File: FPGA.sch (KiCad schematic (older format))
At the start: 5 parts, among them U34 PCA9555AHF, U39 PCA9555AHF

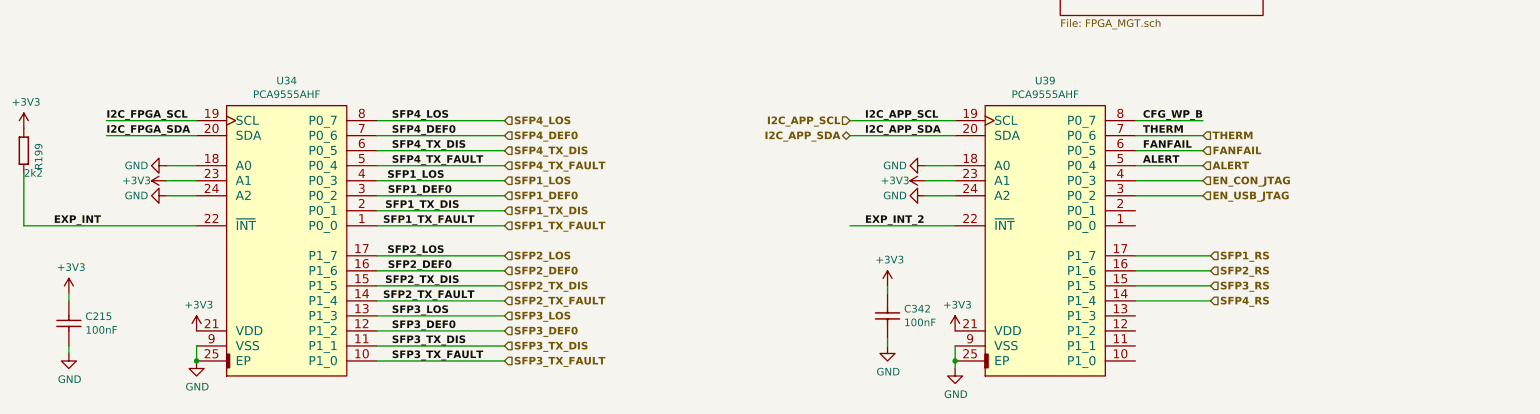
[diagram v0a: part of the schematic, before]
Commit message: LEDs and button added, routed other signals
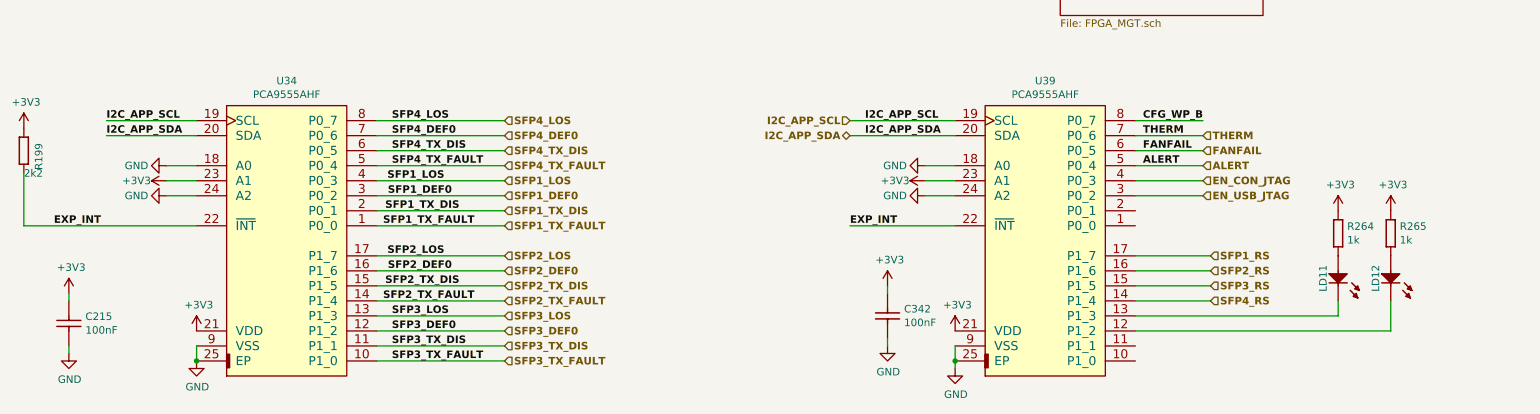
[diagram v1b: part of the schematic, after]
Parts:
- added LD11, LD12: LED_AVAGO_HSMC-C120, ICs And Semiconductors SMD:LED_AVAGO_HSMC-C120, symbol LEDs_&_Displays:LED_AVAGO_HSMC-C120
- added R264, R265: R0402_1K_1%_0.0625W_100PPM, RESC1005X40N, symbol Resistors_SMD:R0402_1K_1%_0.0625W_100PPM
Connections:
- net EXP_INT_2 is gone; now on net EXP_INT: U39.22 (~INT)
- net +3V3: now also R264.1, R265.1
- net I2C_APP_SCL: now also U34.19 (SCL)
- net I2C_APP_SDA: now also U34.20 (SDA)
- net I2C_FPGA_SCL: no longer U34.19 (SCL)
- net I2C_FPGA_SDA: no longer U34.20 (SDA)
- net at U39.12 (P1_2): now also LD12.1 (C)
- net at U39.13 (P1_3): now also LD11.1 (C)
- new net: LD11.2 (A), R264.2
- new net: LD12.2 (A), R265.2

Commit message: bugs fixed
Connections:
- net +3V3: now also U39.18 (A0); no longer U39.23 (A1)
- net GND: now also U39.23 (A1); no longer U39.18 (A0)
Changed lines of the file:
@@
 F0 "FPGA_13_14" 50
 F1 "FPGA_13_14.sch" 50
-F2 "FMC1_N_LA_[0..33]" I R 11450 1850 50
-F3 "FMC1_P_LA_[0..33]" I R 11450 1950 50
-F4 "FMC2_N_LA_[0..33]" I R 11450 2150 50
-F5 "FMC2_P_LA_[0..33]" I R 11450 2250 50
-F6 "CCLK" I L 9950 2100 50
-F7 "CFG_WP_B" O L 9950 2200 50
-F8 "FMC1_CLK1_M2C_P" I R 11450 2700 50
-F9 "FMC1_CLK1_M2C_N" I R 11450 2800 50
-F10 "FMC1_CLK0_M2C_P" I R 11450 2900 50
-F11 "FMC1_CLK0_M2C_N" I R 11450 3000 50
+F2 "CCLK" I L 9950 2100 50
+F3 "CFG_WP_B" O L 9950 2200 50
+F4 "FMC1_CLK1_M2C_P" I R 11450 2700 50
+F5 "FMC1_CLK1_M2C_N" I R 11450 2800 50
+F6 "FMC1_CLK0_M2C_P" I R 11450 2900 50
+F7 "FMC1_CLK0_M2C_N" I R 11450 3000 50
 $EndSheet
 Text HLabel 1750 2050 0    50   BiDi ~ 10
@@
 L power:+3V3 #PWR?
 U 1 1 5C5ED5B2
-P 7100 8750
+P 7100 8650
 AR Path="/5BD32060/5C5ED5B2" Ref="#PWR?"  Part="1"
 AR Path="/5C907554/5C417BCB/5C5ED5B2" Ref="#PWR?"  Part="1"
 AR Path="/5C907554/5C5ED5B2" Ref="#PWR0117"  Part="1"
 AR Path="/5C907554/5CAAC367/5C5ED5B2" Ref="#PWR?"  Part="1"
-F 0 "#PWR0117" H 7100 8600 50  0001 C CNN
-F 1 "+3V3" V 7100 8950 50  0000 C CNN
-F 2 "" H 7100 8750 50  0001 C CNN
-F 3 "" H 7100 8750 50  0001 C CNN
-	1    7100 8750
+F 0 "#PWR0117" H 7100 8500 50  0001 C CNN
+F 1 "+3V3" V 7100 8850 50  0000 C CNN
+F 2 "" H 7100 8650 50  0001 C CNN
+F 3 "" H 7100 8650 50  0001 C CNN
+	1    7100 8650
 	0    -1   -1   0
 $EndComp
@@
 L power:GND #PWR?
 U 1 1 5C5ED5BE
-P 7100 8650
+P 7100 8750
 AR Path="/5BD32060/5C5ED5BE" Ref="#PWR?"  Part="1"
 AR Path="/5BABAC65/5C5ED5BE" Ref="#PWR?"  Part="1"
@@
 AR Path="/5C907554/5C417BCB/5C5ED5BE" Ref="#PWR?"  Part="1"
 AR Path="/5C907554/5C5ED5BE" Ref="#PWR0115"  Part="1"
-F 0 "#PWR0115" H 7100 8400 50  0001 C CNN
-F 1 "GND" V 7100 8450 50  0000 C CNN
-F 2 "" H 7100 8650 50  0001 C CNN
-F 3 "" H 7100 8650 50  0001 C CNN
-	1    7100 8650
+F 0 "#PWR0115" H 7100 8500 50  0001 C CNN
+F 1 "GND" V 7100 8550 50  0000 C CNN
+F 2 "" H 7100 8750 50  0001 C CNN
+F 3 "" H 7100 8750 50  0001 C CNN
+	1    7100 8750
 	0    1    1    0
 $EndComp

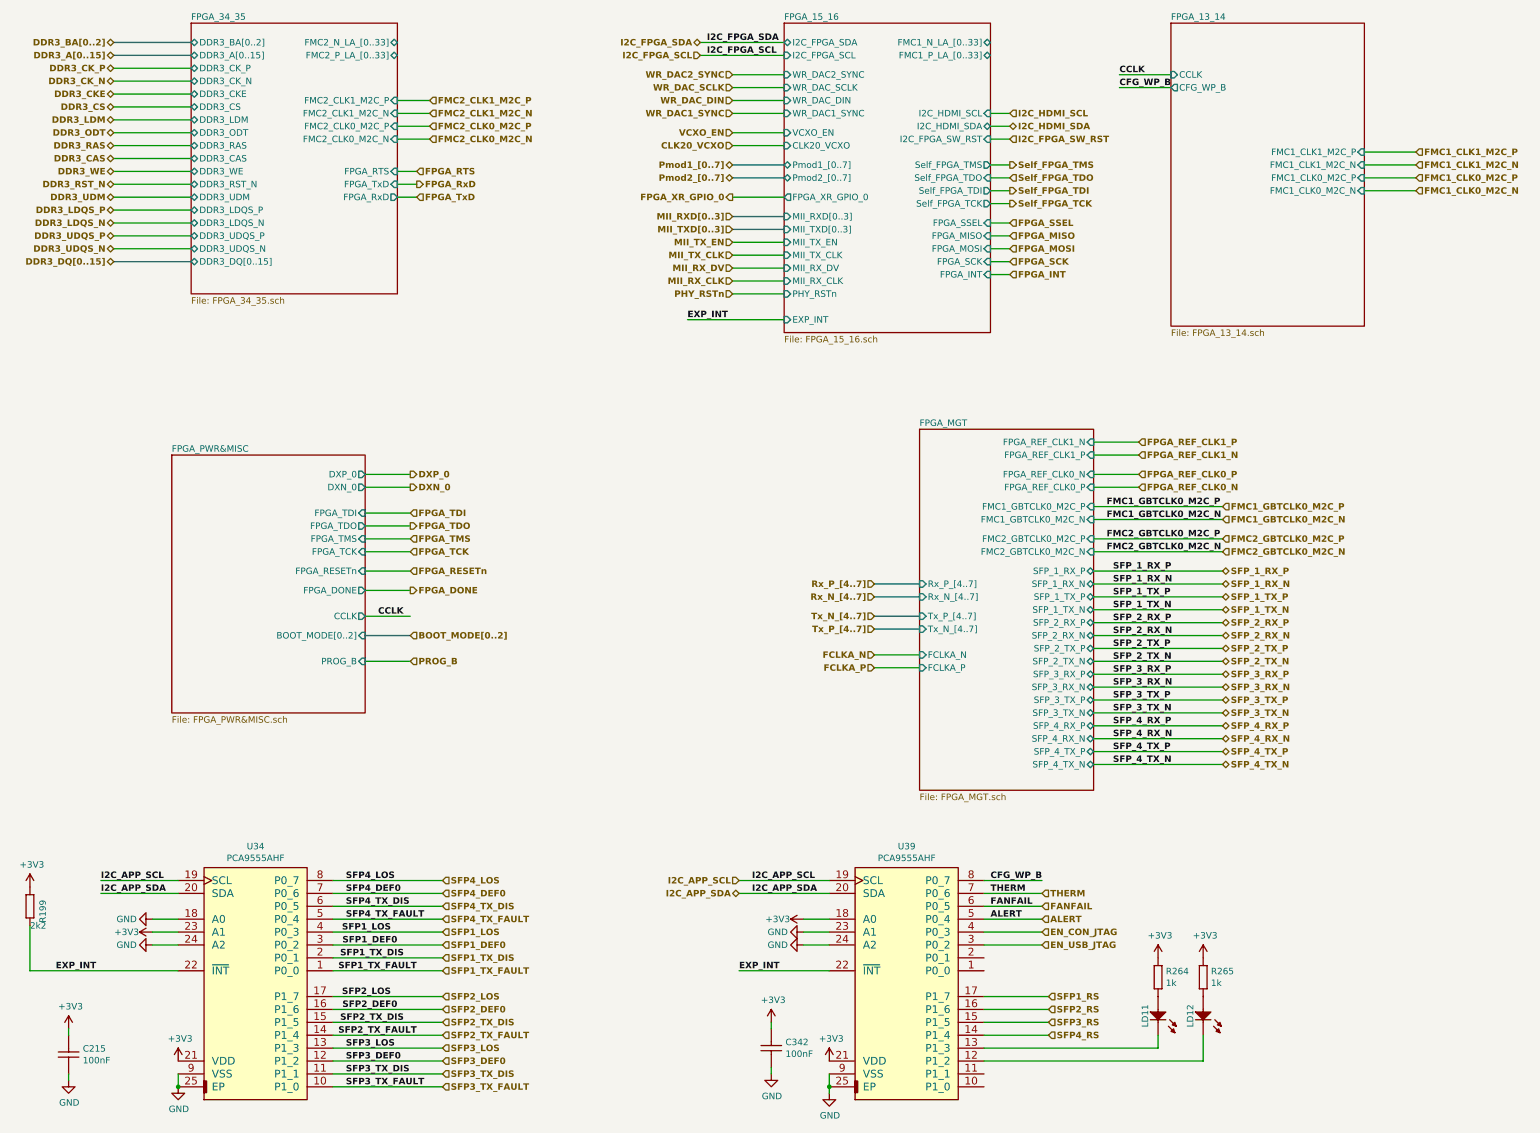
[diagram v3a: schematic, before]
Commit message: new FMC JTAG chain
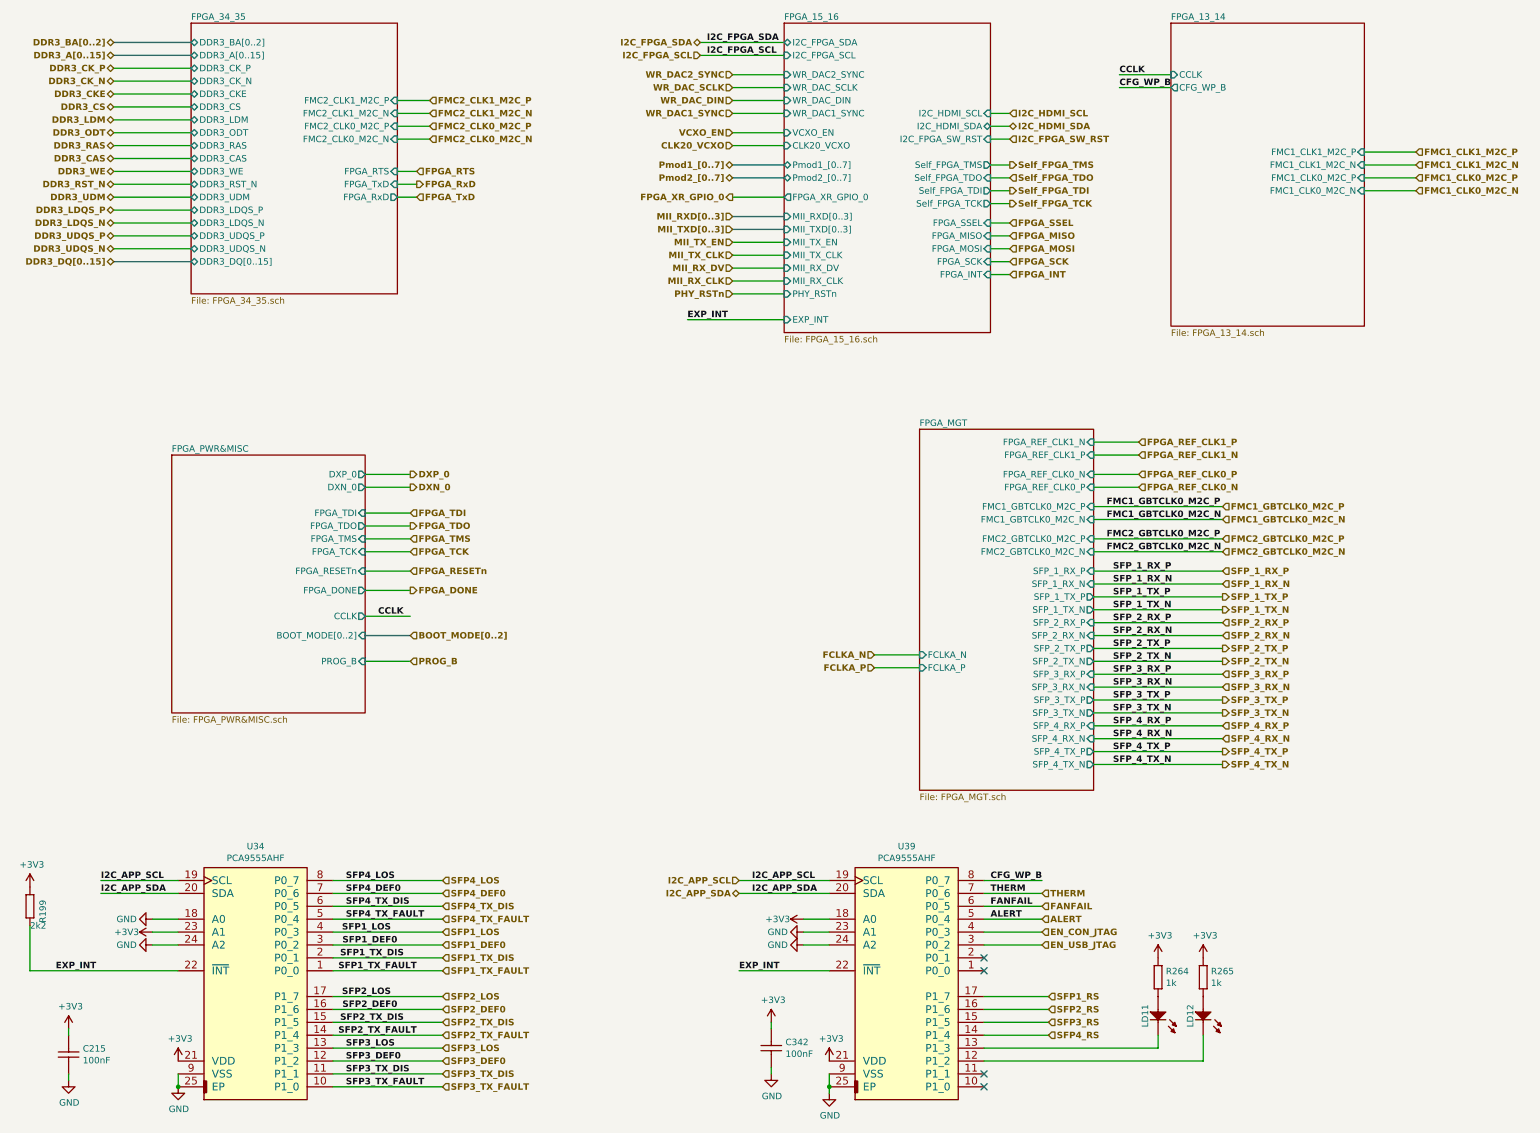
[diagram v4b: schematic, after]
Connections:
- no-connect marks 0 -> 4
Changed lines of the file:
@@
 F8 "FMC2_GBTCLK0_M2C_P" I R 9350 5700 50
 F9 "FMC2_GBTCLK0_M2C_N" I R 9350 5800 50
-F10 "SFP_1_RX_P" B R 9350 5950 50
-F11 "SFP_1_RX_N" B R 9350 6050 50
-F12 "SFP_1_TX_P" B R 9350 6150 50
-F13 "SFP_1_TX_N" B R 9350 6250 50
-F14 "SFP_2_RX_P" B R 9350 6350 50
-F15 "SFP_2_RX_N" B R 9350 6450 50
-F16 "SFP_2_TX_P" B R 9350 6550 50
-F17 "SFP_2_TX_N" B R 9350 6650 50
-F18 "SFP_3_RX_P" B R 9350 6750 50
-F19 "SFP_3_RX_N" B R 9350 6850 50
-F20 "SFP_3_TX_P" B R 9350 6950 50
-F21 "SFP_3_TX_N" B R 9350 7050 50
-F22 "SFP_4_RX_P" B R 9350 7150 50
-F23 "SFP_4_RX_N" B R 9350 7250 50
-F24 "SFP_4_TX_P" B R 9350 7350 50
-F25 "SFP_4_TX_N" B R 9350 7450 50
-F26 "Rx_P_[4..7]" I L 8000 6050 50
-F27 "Rx_N_[4..7]" I L 8000 6150 50
-F28 "Tx_P_[4..7]" I L 8000 6300 50
-F29 "Tx_N_[4..7]" I L 8000 6400 50
+F10 "SFP_1_RX_P" I R 9350 5950 50
+F11 "SFP_1_RX_N" I R 9350 6050 50
+F12 "SFP_1_TX_P" O R 9350 6150 50
+F13 "SFP_1_TX_N" O R 9350 6250 50
+F14 "SFP_2_RX_P" I R 9350 6350 50
+F15 "SFP_2_RX_N" I R 9350 6450 50
+F16 "SFP_2_TX_P" O R 9350 6550 50
+F17 "SFP_2_TX_N" O R 9350 6650 50
+F18 "SFP_3_RX_P" I R 9350 6750 50
+F19 "SFP_3_RX_N" I R 9350 6850 50
+F20 "SFP_3_TX_P" O R 9350 6950 50
+F21 "SFP_3_TX_N" O R 9350 7050 50
+F22 "SFP_4_RX_P" I R 9350 7150 50
+F23 "SFP_4_RX_N" I R 9350 7250 50
+F24 "SFP_4_TX_P" O R 9350 7350 50
+F25 "SFP_4_TX_N" O R 9350 7450 50
 F30 "FCLKA_N" I L 8000 6600 50
 F31 "FCLKA_P" I L 8000 6700 50
@@
 Text Label 9500 6250 0    50   ~ 10
 SFP_1_TX_N
-Text HLabel 10350 5950 2    50   BiDi ~ 10
+Text HLabel 10350 5950 2    50   Input ~ 10
 SFP_1_RX_P
-Text HLabel 10350 6050 2    50   BiDi ~ 10
+Text HLabel 10350 6050 2    50   Input ~ 10
 SFP_1_RX_N
-Text HLabel 10350 6150 2    50   BiDi ~ 10
+Text HLabel 10350 6150 2    50   Output ~ 10
 SFP_1_TX_P
-Text HLabel 10350 6250 2    50   BiDi ~ 10
+Text HLabel 10350 6250 2    50   Output ~ 10
 SFP_1_TX_N
 Text Label 9500 6350 0    50   ~ 10
@@
 Text Label 9500 6650 0    50   ~ 10
 SFP_2_TX_N
-Text HLabel 10350 6350 2    50   BiDi ~ 10
+Text HLabel 10350 6350 2    50   Input ~ 10
 SFP_2_RX_P
-Text HLabel 10350 6450 2    50   BiDi ~ 10
+Text HLabel 10350 6450 2    50   Input ~ 10
 SFP_2_RX_N
-Text HLabel 10350 6550 2    50   BiDi ~ 10
+Text HLabel 10350 6550 2    50   Output ~ 10
 SFP_2_TX_P
-Text HLabel 10350 6650 2    50   BiDi ~ 10
+Text HLabel 10350 6650 2    50   Output ~ 10
 SFP_2_TX_N
 Text Label 9500 6750 0    50   ~ 10
@@
 Text Label 9500 7050 0    50   ~ 10
 SFP_3_TX_N
-Text HLabel 10350 6750 2    50   BiDi ~ 10
+Text HLabel 10350 6750 2    50   Input ~ 10
 SFP_3_RX_P
-Text HLabel 10350 6850 2    50   BiDi ~ 10
+Text HLabel 10350 6850 2    50   Input ~ 10
 SFP_3_RX_N
-Text HLabel 10350 6950 2    50   BiDi ~ 10
+Text HLabel 10350 6950 2    50   Output ~ 10
 SFP_3_TX_P
-Text HLabel 10350 7050 2    50   BiDi ~ 10
+Text HLabel 10350 7050 2    50   Output ~ 10
 SFP_3_TX_N
 Text Label 9500 7150 0    50   ~ 10
@@
 Text Label 9500 7450 0    50   ~ 10
 SFP_4_TX_N
-Text HLabel 10350 7150 2    50   BiDi ~ 10
+Text HLabel 10350 7150 2    50   Input ~ 10
 SFP_4_RX_P
-Text HLabel 10350 7250 2    50   BiDi ~ 10
+Text HLabel 10350 7250 2    50   Input ~ 10
 SFP_4_RX_N
-Text HLabel 10350 7350 2    50   BiDi ~ 10
+Text HLabel 10350 7350 2    50   Output ~ 10
 SFP_4_TX_P
-Text HLabel 10350 7450 2    50   BiDi ~ 10
+Text HLabel 10350 7450 2    50   Output ~ 10
 SFP_4_TX_N
-Text HLabel 7650 6050 0    50   Input ~ 10
-Rx_P_[4..7]
-Text HLabel 7650 6150 0    50   Input ~ 10
-Rx_N_[4..7]
-Text HLabel 7650 6400 0    50   Input ~ 10
-Tx_P_[4..7]
-Text HLabel 7650 6300 0    50   Input ~ 10
-Tx_N_[4..7]
-Wire Bus Line
-	7650 6050 8000 6050
-Wire Bus Line
-	7650 6150 8000 6150
-Wire Bus Line
-	7650 6300 8000 6300
-Wire Bus Line
-	7650 6400 8000 6400
 Wire Wire Line
 	9350 5950 10350 5950
@@
 F18 "DDR3_UDQS_N" B L 2350 3450 50
 F19 "DDR3_DQ[0..15]" B L 2350 3550 50
-F20 "FMC2_N_LA_[0..33]" B R 3950 1850 50
-F21 "FMC2_P_LA_[0..33]" B R 3950 1950 50
 F22 "FMC2_CLK1_M2C_P" I R 3950 2300 50
 F23 "FMC2_CLK1_M2C_N" I R 3950 2400 50
@@
 F0 "FPGA_15_16" 50
 F1 "FPGA_15_16.sch" 50
-F2 "FMC1_N_LA_[0..33]" B R 8550 1850 50
-F3 "FMC1_P_LA_[0..33]" B R 8550 1950 50
 F4 "I2C_FPGA_SDA" B L 6950 1850 50
 F5 "I2C_FPGA_SCL" I L 6950 1950 50
@@
 Text Label 1650 8450 0    50   ~ 10
 I2C_APP_SDA
+NoConn ~ 8500 8950
+NoConn ~ 8500 9050
+NoConn ~ 8500 9850
+NoConn ~ 8500 9950
 $EndSCHEMATC
